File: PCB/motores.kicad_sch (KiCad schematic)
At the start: 28 parts, among them IC2 IR2175STRPBF, J10 Conn_01x03, J11 Conn_01x03, J6 WINDOW, J7 DOOR, J8 Conn_01x02, J9 Conn_01x02, K1 G6E, K2 G6E, K3 G6E, K4 G6E, Q1 AO3401A, Q2 AO3401A, Q3 AO3401A, Q4 AO3401A

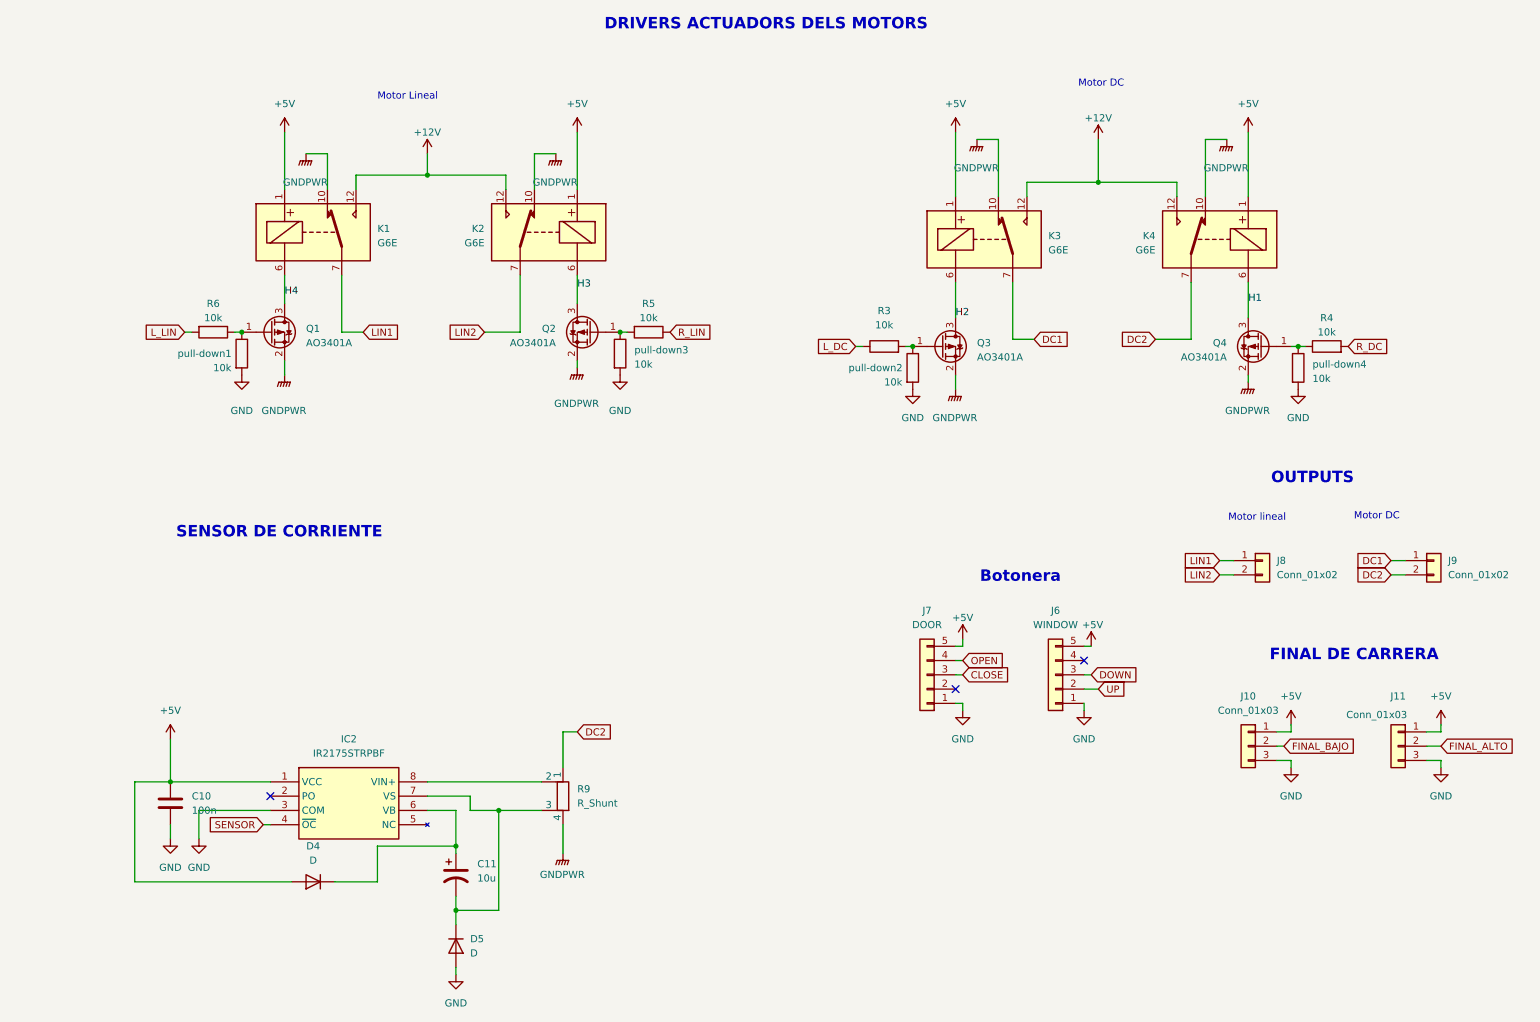
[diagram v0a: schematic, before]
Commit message: Terminales y Diodos
Terminales de motor tipo screw y diodos de relés
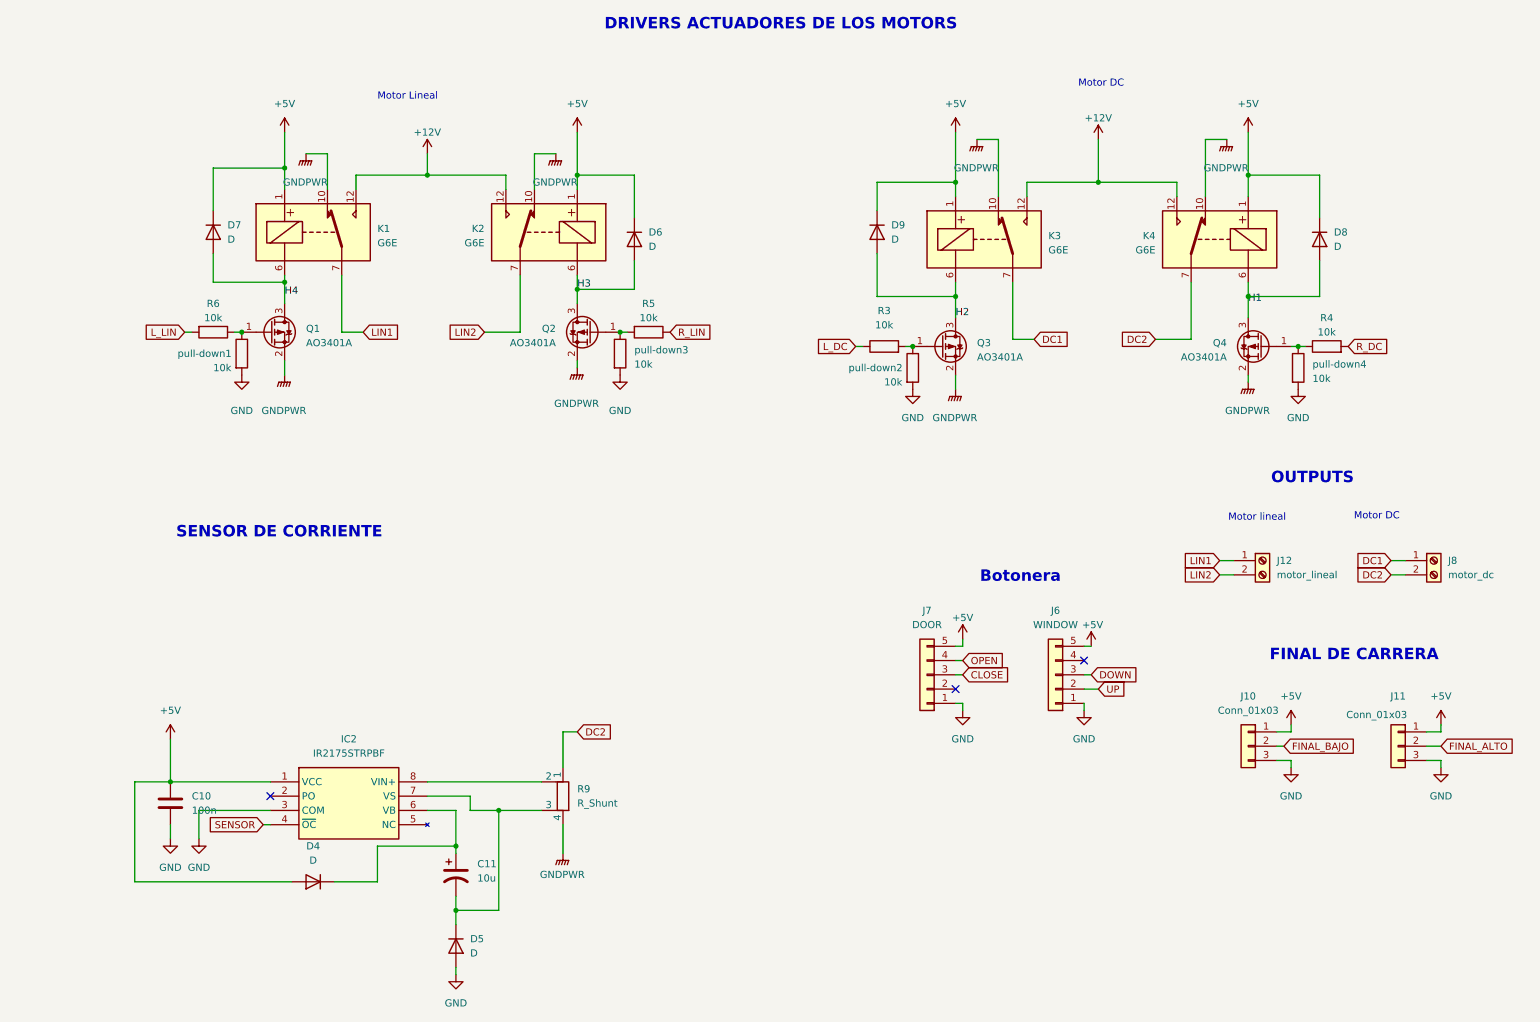
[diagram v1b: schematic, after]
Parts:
- removed J8, J9: Conn_01x02, symbol Connector_Generic:Conn_01x02
- added D6, D7, D8, D9: D, symbol Device:D
- added J12: motor_lineal, symbol Connector:Screw_Terminal_01x02
- added J8: motor_dc, symbol Connector:Screw_Terminal_01x02
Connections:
- net +5V: now also D6.1 (K), D7.1 (K), D8.1 (K), D9.1 (K)
- net DC1: now also J8.1 (Pin_1)
- net DC2: now also J8.2 (Pin_2)
- net H1: now also D8.2 (A)
- net H2: now also D9.2 (A)
- net H3: now also D6.2 (A)
- net H4: now also D7.2 (A)
- net LIN1: now also J12.1 (Pin_1)
- net LIN2: now also J12.2 (Pin_2)
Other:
- note added: "DRIVERS ACTUADORES DE LOS MOTORS"
- note removed: "DRIVERS ACTUADORS DELS MOTORS"

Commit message: Update motores.kicad_sch
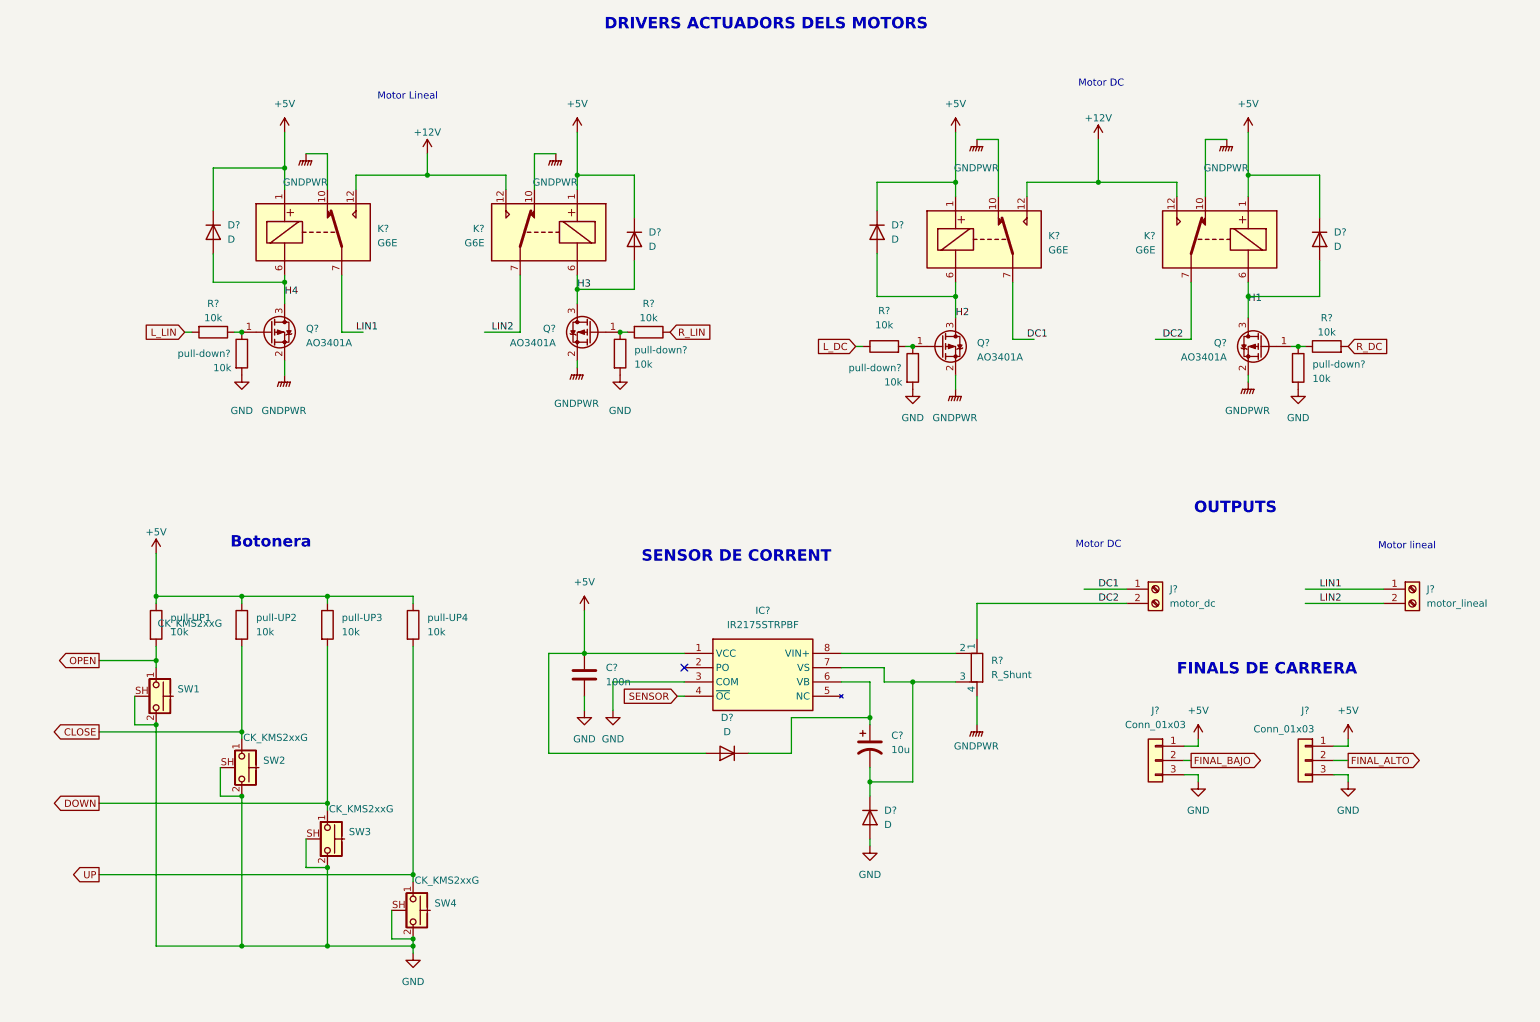
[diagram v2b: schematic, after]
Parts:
- removed J6: WINDOW, Connector_PinHeader_2.54mm:PinHeader_1x05_P2.54mm_Vertical, symbol Connector_Generic:Conn_01x05
- removed J7: DOOR, Connector_PinHeader_2.54mm:PinHeader_1x05_P2.54mm_Vertical, symbol Connector_Generic:Conn_01x05
- added SW1, SW2, SW3, SW4: CK_KMS2xxG, Button_Switch_SMD:SW_SPST_CK_KMS2xxGP, symbol Switch:CK_KMS2xxG
- added pull-UP1, pull-UP2, pull-UP3, pull-UP4: 10k, Resistor_SMD:R_1206_3216Metric_Pad1.30x1.75mm_HandSolder, symbol Device:R
- renumbered C11 to C?, C10 to C?, D6 to D?, D5 to D?, D9 to D?, D7 to D?, D8 to D?, D4 to D?, IC2 to IC?, J8 to J?, J11 to J?, J12 to J?, J10 to J?, K2 to K?, K1 to K?, K3 to K?, K4 to K?, Q4 to Q?, Q1 to Q?, Q2 to Q?, Q3 to Q?, R6 to R?, R9 to R?, R3 to R?, R5 to R?, R4 to R?, pull-down3 to pull-down?, pull-down4 to pull-down?, pull-down2 to pull-down?, pull-down1 to pull-down?
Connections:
- net +5V: now also pull-UP1.1, pull-UP2.1, pull-UP3.1, pull-UP4.1
- net CLOSE: now also SW2.1, pull-UP2.2
- net DOWN: now also SW3.1, pull-UP3.2
- net GND: now also SW1.2, SW1.SH (B), SW2.2, SW2.SH (B), SW3.2, SW3.SH (B), SW4.2, SW4.SH (B)
- net OPEN: now also SW1.1, pull-UP1.2
- net UP: now also SW4.1, pull-UP4.2
- no-connect marks 3 -> 1
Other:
- note added: "DRIVERS ACTUADORS DELS MOTORS"
- note added: "FINALS DE CARRERA"
- note added: "SENSOR DE CORRENT"
- note removed: "DRIVERS ACTUADORES DE LOS MOTORS"
- note removed: "FINAL DE CARRERA"
- note removed: "SENSOR DE CORRIENTE"
- moved on the sheet: C?, D?, IC?, J?, R?

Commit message: conectados directamente los relés a los conectores
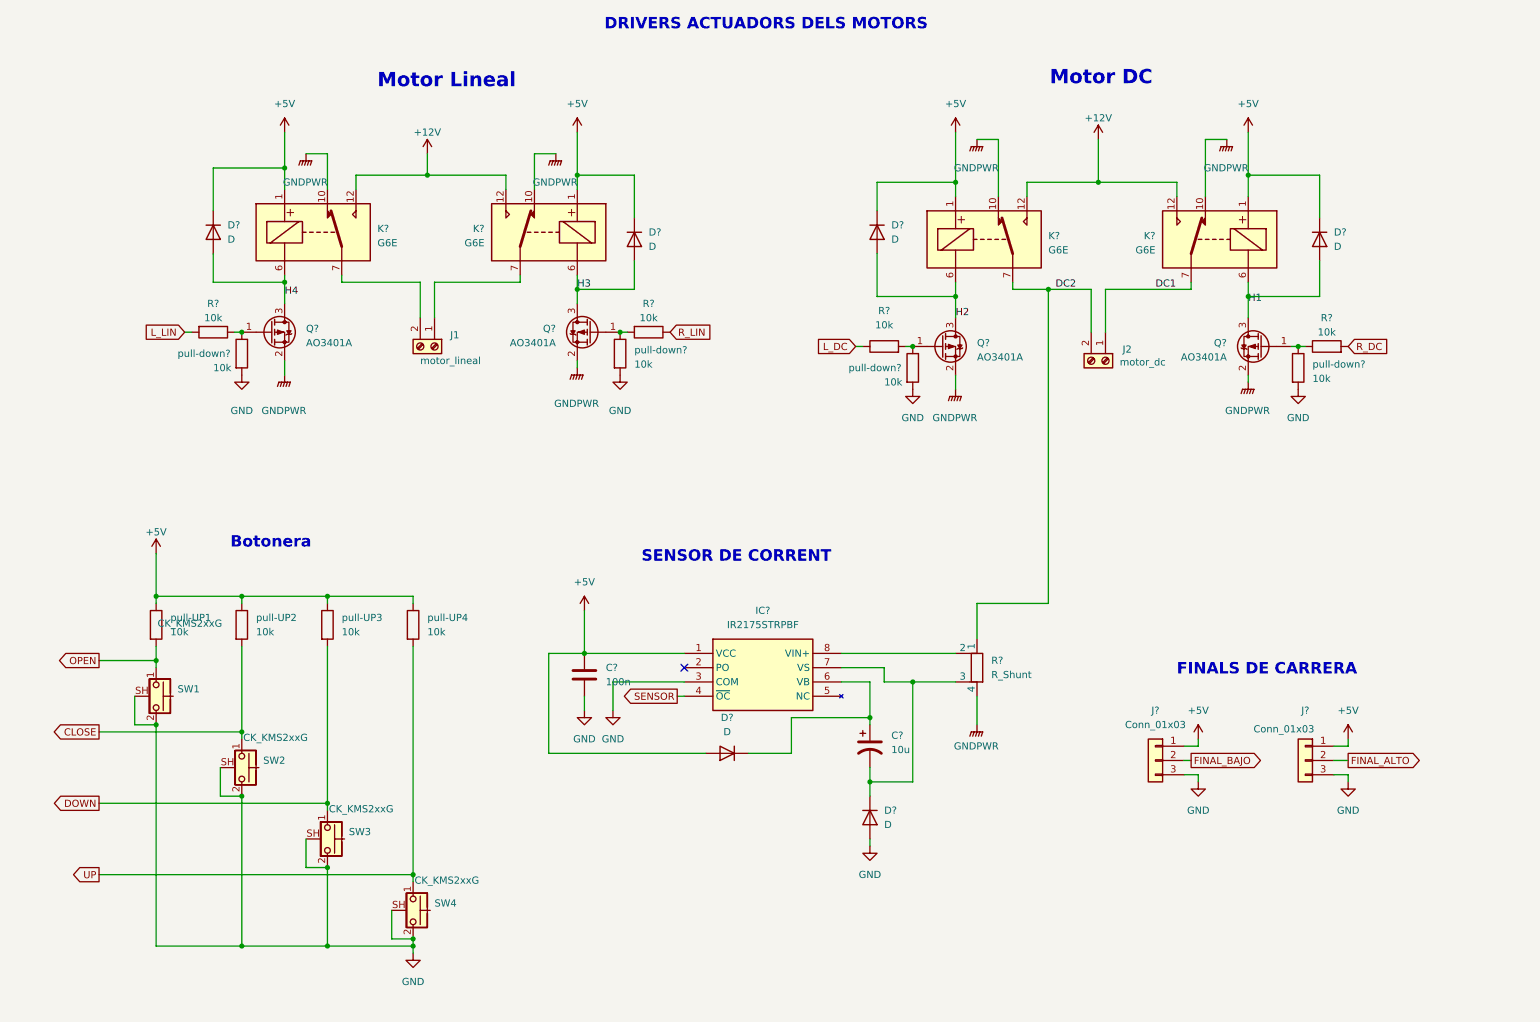
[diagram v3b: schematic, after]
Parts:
- removed J?: motor_dc, symbol Connector:Screw_Terminal_01x02
- removed J?: motor_lineal, symbol Connector:Screw_Terminal_01x02
- added J1: motor_lineal, symbol Connector:Screw_Terminal_01x02
- added J2: motor_dc, symbol Connector:Screw_Terminal_01x02
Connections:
- net DC1: now also K?.7, J2.1 (Pin_1); no longer K?.7
- net DC2: now also K?.7, J2.2 (Pin_2); no longer K?.7
- net LIN1: no longer names the net of K?.7
- net LIN1: now also J1.2 (Pin_2)
- net LIN2: no longer names the net of K?.7
- net LIN2: now also J1.1 (Pin_1)
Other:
- note removed: "Motor lineal"
- note removed: "OUTPUTS"

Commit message: anadido el shdn directo al PIC. Es un pin de alarma térmica del transceiver. El sensor de corriente está mal hay que darle una vuelta
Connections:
- net DC1 renamed LS
- net LS: now also R?.1
- net DC2 renamed HS
- net HS: no longer R?.1
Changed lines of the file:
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@@
 	)
 	(junction
+		(at 214.63 67.31)
+		(diameter 0)
+		(color 0 0 0 0)
+	)
+	(junction
 		(at 67.31 158.75)
 		(diameter 0)
@@
 	)
 	(junction
-		(at 195.58 67.31)
-		(diameter 0)
-		(color 0 0 0 0)
-	)
-	(junction
 		(at 231.14 68.58)
 		(diameter 0)
@@
 	(wire
 		(pts
-			(xy 182.88 123.19) (xy 195.58 123.19)
+			(xy 182.88 123.19) (xy 214.63 123.19)
 		)
 		(stroke
@@
 	(wire
 		(pts
-			(xy 205.74 67.31) (xy 220.98 67.31)
+			(xy 205.74 67.31) (xy 214.63 67.31)
 		)
 		(stroke
@@
 	(wire
 		(pts
-			(xy 195.58 123.19) (xy 195.58 67.31)
+			(xy 214.63 67.31) (xy 220.98 67.31)
 		)
 		(stroke
@@
 	(wire
 		(pts
-			(xy 195.58 67.31) (xy 203.2 67.31)
-		)
-		(stroke
-			(width 0)
-			(type default)
-		)
-	)
-	(wire
-		(pts
 			(xy 222.25 153.67) (xy 222.25 154.94)
 		)
@@
 	(wire
 		(pts
-			(xy 189.23 67.31) (xy 195.58 67.31)
+			(xy 189.23 67.31) (xy 203.2 67.31)
+		)
+		(stroke
+			(width 0)
+			(type default)
+		)
+	)
+	(wire
+		(pts
+			(xy 214.63 67.31) (xy 214.63 123.19)
 		)
 		(stroke
@@
 		)
 	)
-	(label "DC2"
+	(label "HS"
 		(at 196.85 67.31 0)
 		(effects
@@
 		)
 	)
-	(label "DC1"
+	(label "LS"
 		(at 214.63 67.31 0)
 		(effects
@@
 				)
 			)
+			(project "puertas"
+				(path "/c96004bd-c0fc-431c-a510-eb1e1a82944f/9d8869dd-b067-4c66-a8ca-a407ea6f90ea"
+					(reference "#PWR0103")
+					(unit 1)
+				)
+			)
 		)
 	)
@@
 				)
 			)
+			(project "puertas"
+				(path "/c96004bd-c0fc-431c-a510-eb1e1a82944f/9d8869dd-b067-4c66-a8ca-a407ea6f90ea"
+					(reference "SW?")
+					(unit 1)
+				)
+			)
 		)
 	)
@@
 				)
 			)
+			(project "puertas"
+				(path "/c96004bd-c0fc-431c-a510-eb1e1a82944f/9d8869dd-b067-4c66-a8ca-a407ea6f90ea"
+					(reference "pull-UP?")
+					(unit 1)
+				)
+			)
 		)
 	)
@@
 				)
 			)
+			(project "puertas"
+				(path "/c96004bd-c0fc-431c-a510-eb1e1a82944f/9d8869dd-b067-4c66-a8ca-a407ea6f90ea"
+					(reference "pull-UP?")
+					(unit 1)
+				)
+			)
 		)
 	)
@@
 				)
 			)
+			(project "puertas"
+				(path "/c96004bd-c0fc-431c-a510-eb1e1a82944f/9d8869dd-b067-4c66-a8ca-a407ea6f90ea"
+					(reference "J?")
+					(unit 1)
+				)
+			)
 		)
 	)
@@
 				)
 			)
+			(project "puertas"
+				(path "/c96004bd-c0fc-431c-a510-eb1e1a82944f/9d8869dd-b067-4c66-a8ca-a407ea6f90ea"
+					(reference "J?")
+					(unit 1)
+				)
+			)
 		)
 	)
@@
 				)
 			)
+			(project "puertas"
+				(path "/c96004bd-c0fc-431c-a510-eb1e1a82944f/9d8869dd-b067-4c66-a8ca-a407ea6f90ea"
+					(reference "pull-UP?")
+					(unit 1)
+				)
+			)
 		)
 	)
@@
 				)
 			)
+			(project "puertas"
+				(path "/c96004bd-c0fc-431c-a510-eb1e1a82944f/9d8869dd-b067-4c66-a8ca-a407ea6f90ea"
+					(reference "SW?")
+					(unit 1)
+				)
+			)
 		)
 	)
@@
 				)
 			)
+			(project "puertas"
+				(path "/c96004bd-c0fc-431c-a510-eb1e1a82944f/9d8869dd-b067-4c66-a8ca-a407ea6f90ea"
+					(reference "SW?")
+					(unit 1)
+				)
+			)
 		)
 	)
@@
 				)
 			)
+			(project "puertas"
+				(path "/c96004bd-c0fc-431c-a510-eb1e1a82944f/9d8869dd-b067-4c66-a8ca-a407ea6f90ea"
+					(reference "SW?")
+					(unit 1)
+				)
+			)
 		)
 	)
@@
 				)
 			)
+			(project "puertas"
+				(path "/c96004bd-c0fc-431c-a510-eb1e1a82944f/9d8869dd-b067-4c66-a8ca-a407ea6f90ea"
+					(reference "#PWR0104")
+					(unit 1)
+				)
+			)
 		)
 	)
@@
 					(unit 1)
 				)
+			)
+			(project "puertas"
+				(path "/c96004bd-c0fc-431c-a510-eb1e1a82944f/9d8869dd-b067-4c66-a8ca-a407ea6f90ea"
+					(reference "pull-UP?")
+					(unit 1)
+				)

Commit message: Add files via upload
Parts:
- removed SW1, SW2, SW3, SW4: CK_KMS2xxG, Button_Switch_SMD:SW_SPST_CK_KMS2xxGP, symbol Switch:CK_KMS2xxG
- removed pull-UP1, pull-UP2, pull-UP3, pull-UP4: 10k, Resistor_SMD:R_1206_3216Metric_Pad1.30x1.75mm_HandSolder, symbol Device:R
- C10: renamed from C?; footprint (none) -> Capacitor_SMD:C_1206_3216Metric
- C11: renamed from C?; footprint (none) -> Capacitor_THT:CP_Radial_D6.3mm_P2.50mm
- D4, D5, D6, D7, D8, D9: renamed from D?; footprint (none) -> Diode_THT:D_DO-201AD_P12.70mm_Horizontal
- IC2: renamed from IC?; footprint SOIC127P600X175-8N -> IR2175STRPBF:SOIC127P600X175-8N
- J10, J11: renamed from J?; footprint (none) -> Connector_PinHeader_2.54mm:PinHeader_1x03_P2.54mm_Vertical
- J12: renamed from J2; footprint (none) -> TerminalBlock_Phoenix:TerminalBlock_Phoenix_MPT-0,5-2-2.54_1x02_P2.54mm_Horizontal
- J9: renamed from J1; footprint (none) -> TerminalBlock_Phoenix:TerminalBlock_Phoenix_MPT-0,5-2-2.54_1x02_P2.54mm_Horizontal
- R3: renamed from R?; footprint (none) -> Resistor_SMD:R_1206_3216Metric
- R4, R5, R6: renamed from R?; footprint Resistor_SMD:R_1206_3216Metric_Pad1.30x1.75mm_HandSolder -> Resistor_SMD:R_1206_3216Metric
- R9: renamed from R?; footprint (none) -> Resistor_SMD:R_Shunt_Ohmite_LVK25
- pull-down1, pull-down2, pull-down3, pull-down4: renamed from pull-down?; footprint Resistor_SMD:R_1206_3216Metric_Pad1.30x1.75mm_HandSolder -> Capacitor_SMD:C_1206_3216Metric
- gave numbers to parts that had none: 8
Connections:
- net LIN2: now reaches J9.1 (Pin_1), K2.7
- net LIN1: now reaches J9.2 (Pin_2), K1.7
- net HS renamed DC1
- net LS renamed DC2
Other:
- note added: "SENSOR DE CORRIENTE"
- note removed: "Botonera"
- note removed: "SENSOR DE CORRENT"
- moved on the sheet: C10, C11, D4, D5, IC2, J10, J11, R9

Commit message: esquemático  v2
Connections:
- net R_MOSDC2: now reaches Q4.1 (G), R4.1, pull-down4.1
- net R_MOSL1: now reaches Q1.1 (G), R6.1, pull-down1.1
- net VS: now reaches C11.2, D5.1 (K), IC2.7 (VS), R9.3
- net R_MOSL2: now reaches Q2.1 (G), R5.2, pull-down3.1
- net R_MOSDC1: now reaches Q3.1 (G), R3.2, pull-down2.1
- net VIN+: now reaches IC2.8 (VIN+), R9.2
- net VB: now reaches C11.1, D4.1 (K), IC2.6 (VB)
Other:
- moved on the sheet: C10, C11, D4, D5, D6, D7, D8, D9, IC2, J10, J11, J12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
